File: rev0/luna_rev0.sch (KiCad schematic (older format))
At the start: 37 parts, among them J1 USB_B_Micro, J2 USB_B_Micro, J3 USB_A, J4 USB_B_Micro, J7 Conn_02x02_Counter_Clockwise, J8 Conn_Coaxial, J9 Conn_Coaxial, SW1 BTN_DFU, SW2 BTN_RESET, U1 AP22814-SOT, U12 AP22814-SOT, Y1 Osc60MHz

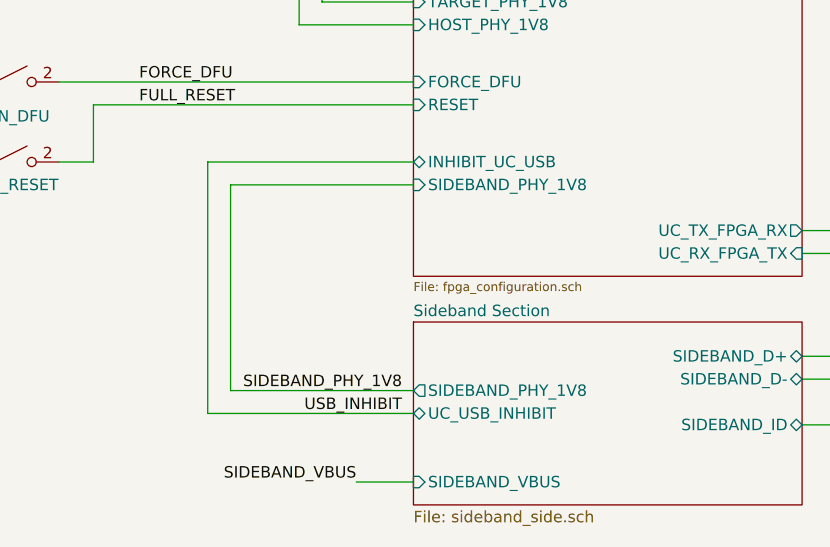
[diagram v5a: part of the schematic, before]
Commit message: hardware: add FPGA self-program option
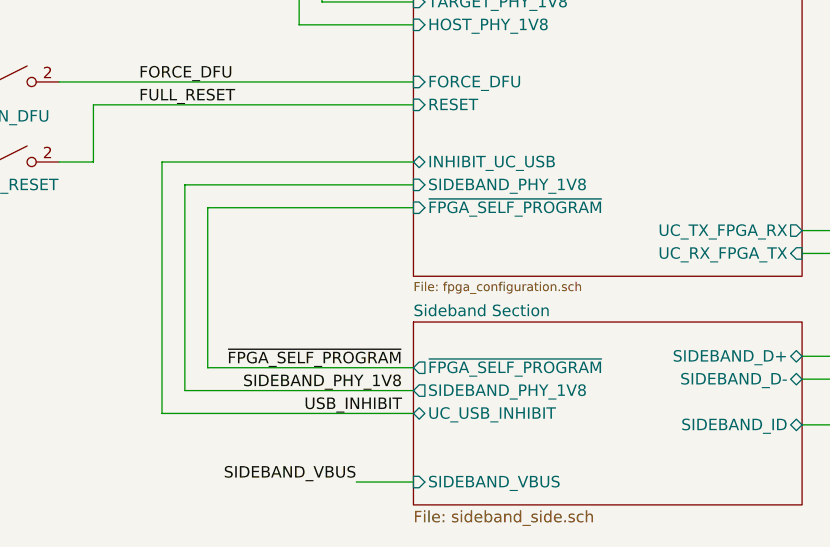
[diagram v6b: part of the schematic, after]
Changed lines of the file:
@@
 F1 "power_supplies.sch" 50
-$EndSheet
-$Sheet
-S 4000 4900 1700 1500
-U 5DCAA6D2
-F0 "FPGA Configuration and Dev Features" 39
-F1 "fpga_configuration.sch" 39
-F2 "SIDEBAND_D-" B R 5700 5150 50
-F3 "SIDEBAND_D+" B R 5700 5050 50
-F4 "SIDEBAND_PHY_1V8" I L 4000 6000 50
-F5 "HOST_PHY_1V8" I L 4000 5300 50
-F6 "TARGET_PHY_1V8" I L 4000 5200 50
-F7 "FORCE_DFU" I L 4000 5550 50
-F8 "INHIBIT_UC_USB" B L 4000 5900 50
-F9 "RESET" I L 4000 5650 50
-F10 "UC_TX_FPGA_RX" O R 5700 6200 50
-F11 "UC_RX_FPGA_TX" I R 5700 6300 50
 $EndSheet
 Text Label 5950 5050 0    50   ~ 0
@@
 F6 "SIDEBAND_ID" B R 5700 7050 50
 F7 "UC_USB_INHIBIT" B L 4000 7000 50
+F8 "~FPGA_SELF_PROGRAM" O L 4000 6800 50
 $EndSheet
 Wire Wire Line
-	4000 6900 3200 6900
+	4000 6900 3000 6900
 Wire Wire Line
 	6500 4850 6500 4600
@@
 $EndComp
 Wire Wire Line
-	3200 6900 3200 6000
+	3000 6900 3000 6000
 Wire Wire Line
 	3500 5300 4000 5300
@@
 HOST_ID
 Wire Wire Line
-	4000 6000 3200 6000
+	4000 6000 3000 6000
 $Comp
 L Switch:SW_SPST SW1
@@
 $EndSheet
 Wire Wire Line
-	4000 7000 3100 7000
-Wire Wire Line
-	3100 7000 3100 5900
-Wire Wire Line
-	3100 5900 4000 5900
+	4000 7000 2900 7000
+Wire Wire Line
+	2900 7000 2900 5900
+Wire Wire Line
+	2900 5900 4000 5900
 Text Label 3950 7000 2    50   ~ 0
 USB_INHIBIT
@@
 Wire Wire Line
 	9750 5750 9950 5750
+$Sheet
+S 4000 4900 1700 1500
+U 5DCAA6D2
+F0 "FPGA Configuration and Dev Features" 39
+F1 "fpga_configuration.sch" 39
+F2 "SIDEBAND_D-" B R 5700 5150 50
+F3 "SIDEBAND_D+" B R 5700 5050 50
+F4 "SIDEBAND_PHY_1V8" I L 4000 6000 50
+F5 "HOST_PHY_1V8" I L 4000 5300 50
+F6 "TARGET_PHY_1V8" I L 4000 5200 50
+F7 "FORCE_DFU" I L 4000 5550 50
+F8 "INHIBIT_UC_USB" B L 4000 5900 50
+F9 "RESET" I L 4000 5650 50
+F10 "UC_TX_FPGA_RX" O R 5700 6200 50
+F11 "UC_RX_FPGA_TX" I R 5700 6300 50
+F12 "~FPGA_SELF_PROGRAM" I L 4000 6100 50
+$EndSheet
+Wire Wire Line
+	4000 6800 3100 6800
+Wire Wire Line
+	3100 6800 3100 6100
+Wire Wire Line
+	3100 6100 4000 6100
+Text Label 3950 6800 2    50   ~ 0
+~FPGA_SELF_PROGRAM
 $EndSCHEMATC

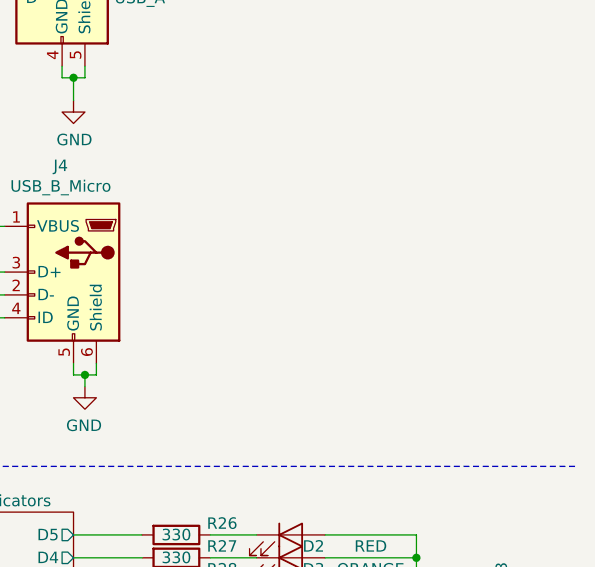
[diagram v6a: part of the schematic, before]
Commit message: hardware: change J3 part selection to Jing C42504
Footprint is designed for Kycon KUSBXHT-SB-AS1N-B30-NF in order to fit a
wide variety of compatible parts.
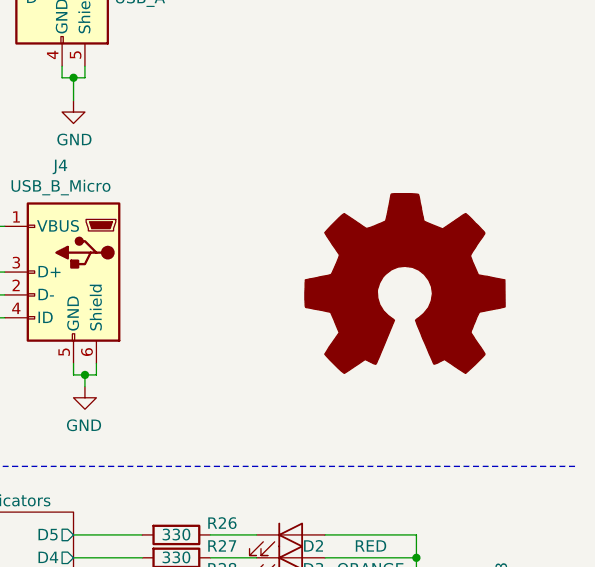
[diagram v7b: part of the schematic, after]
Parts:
- J3: footprint luna:CONN-Amphenol-UE27AC54100 -> luna:USB_A_Kycon_KUSBXHT-SB-AS1N-B30-NF_Horizontal; Description CONN RCPT USB2.0 TYPEA 4POS R/A -> USB A TYPE RECEPTACLE, SHORT BODY; Manufacturer Amphenol ICC -> Jing Extension of the Electronic Co.; Part Number UE27AC54100 -> C42504
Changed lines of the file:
@@
 Sheet 1 9
 Title "LUNA USB Multitool"
-Date "2020-05-21"
+Date "2020-12-07"
 Rev "r0"
 Comp "Copyright 2019-2020 Great Scott Gadgets"
@@
 Wire Wire Line
 	8950 2850 8950 2900
-$Comp
-L Connector:USB_A J3
-U 1 1 5DD6DEF2
-P 8950 2450
-F 0 "J3" H 8721 2439 50  0000 R CNN
-F 1 "USB_A" H 8721 2349 50  0000 R CNN
-F 2 "luna:CONN-Amphenol-UE27AC54100" H 9100 2400 50  0001 C CNN
-F 3 " ~" H 9100 2400 50  0001 C CNN
-F 4 "CONN RCPT USB2.0 TYPEA 4POS R/A" H 8950 2450 50  0001 C CNN "Description"
-F 5 "Amphenol ICC" H 8950 2450 50  0001 C CNN "Manufacturer"
-F 6 "UE27AC54100" H 8950 2450 50  0001 C CNN "Part Number"
-	1    8950 2450
-	-1   0    0    -1
-$EndComp
 Wire Wire Line
 	4000 3500 3600 3500
@@
 Text Label 3950 6800 2    50   ~ 0
 ~FPGA_SELF_PROGRAM
+$Comp
+L Graphic:Logo_Open_Hardware_Large #LOGO1
+U 1 1 5FCC45F6
+P 10450 3850
+F 0 "#LOGO1" H 10450 4350 50  0001 C CNN
+F 1 "Logo_Open_Hardware_Large" H 10450 3450 50  0001 C CNN
+F 2 "" H 10450 3850 50  0001 C CNN
+F 3 "~" H 10450 3850 50  0001 C CNN
+	1    10450 3850
+	1    0    0    -1
+$EndComp
+$Comp
+L Connector:USB_A J3
+U 1 1 5DD6DEF2
+P 8950 2450
+F 0 "J3" H 8721 2439 50  0000 R CNN
+F 1 "USB_A" H 8721 2349 50  0000 R CNN
+F 2 "luna:USB_A_Kycon_KUSBXHT-SB-AS1N-B30-NF_Horizontal" H 9100 2400 50  0001 C CNN
+F 3 " ~" H 9100 2400 50  0001 C CNN
+F 4 "USB A TYPE RECEPTACLE, SHORT BODY" H 8950 2450 50  0001 C CNN "Description"
+F 5 "Jing Extension of the Electronic Co." H 8950 2450 50  0001 C CNN "Manufacturer"
+F 6 "C42504" H 8950 2450 50  0001 C CNN "Part Number"
+	1    8950 2450
+	-1   0    0    -1
+$EndComp
 $EndSCHEMATC

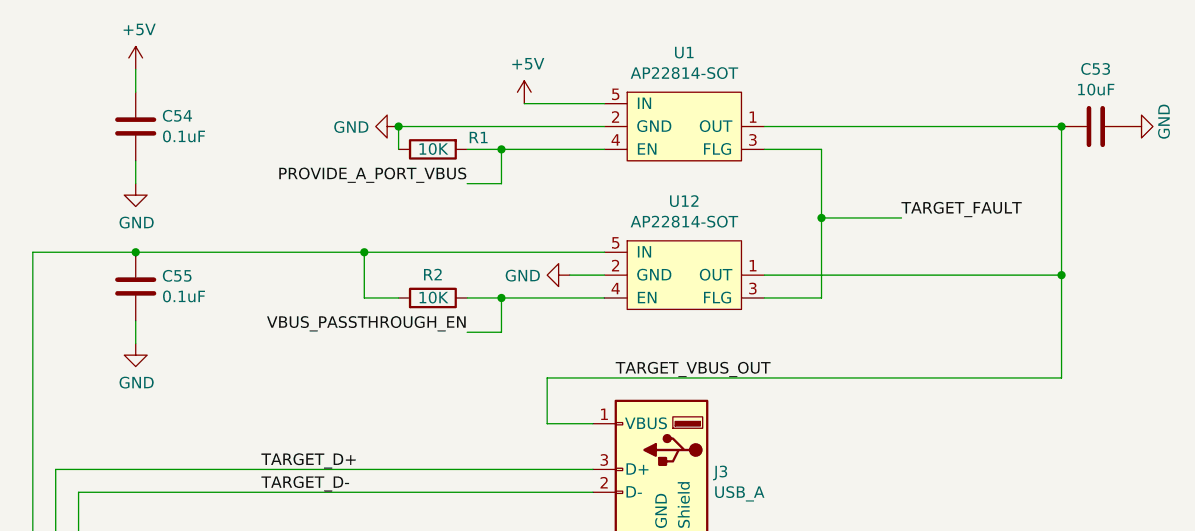
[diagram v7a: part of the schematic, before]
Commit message: hardware: fix load switch oscillation by decreasing R1 and R2 values
update load switch input and output capacitors
add GND zone on In2.Cu under J3 data signals
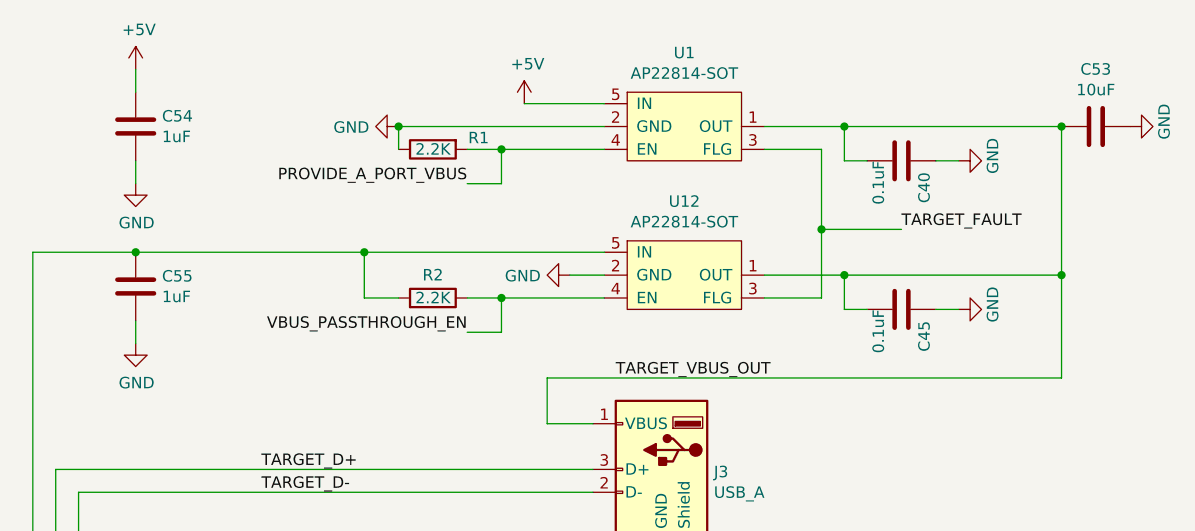
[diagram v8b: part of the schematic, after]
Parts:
- added C40, C45: 0.1uF, Capacitor_SMD:C_0402_1005Metric, symbol Device:C
- C54, C55: value 0.1uF -> 1uF; footprint Capacitor_SMD:C_0402_1005Metric -> Capacitor_SMD:C_0603_1608Metric; Part Number GENERIC-CAP-0402-0.1uF -> GENERIC-CAP-0603-1uF
- R1, R2: value 10K -> 2.2K; Part Number GENERIC-RES-0402-10K -> GENERIC-RES-0402-2.2K
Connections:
- net GND: now also C40.1, C45.1
- net TARGET_VBUS_OUT: now also C40.2, C45.2
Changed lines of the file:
@@
 Wire Wire Line
 	8550 1600 8700 1600
-Text Label 10000 1350 0    50   ~ 0
+Text Label 10000 1400 0    50   ~ 0
 TARGET_FAULT
 Text Label 8100 1200 2    50   ~ 0
@@
 P 7950 1700
 F 0 "R2" V 8050 1700 50  0000 C CNN
-F 1 "10K" V 7950 1700 50  0000 C CNN
+F 1 "2.2K" V 7950 1700 50  0000 C CNN
 F 2 "Resistor_SMD:R_0402_1005Metric" V 7880 1700 50  0001 C CNN
 F 3 "~" H 7950 1700 50  0001 C CNN
-F 4 "GENERIC-RES-0402-10K" H 7950 1700 50  0001 C CNN "Part Number"
+F 4 "GENERIC-RES-0402-2.2K" H 7950 1700 50  0001 C CNN "Part Number"
 	1    7950 1700
 	0    1    -1   0
@@
 $EndComp
 Wire Wire Line
-	9400 1600 10700 1600
+	9400 1600 9750 1600
 Wire Wire Line
 	10700 1600 10700 2050
@@
 P 7950 1050
 F 0 "R1" V 7900 850 50  0000 C CNN
-F 1 "10K" V 7950 1050 50  0000 C CNN
+F 1 "2.2K" V 7950 1050 50  0000 C CNN
 F 2 "Resistor_SMD:R_0402_1005Metric" V 7880 1050 50  0001 C CNN
 F 3 "~" H 7950 1050 50  0001 C CNN
-F 4 "GENERIC-RES-0402-10K" H 7950 1050 50  0001 C CNN "Part Number"
+F 4 "GENERIC-RES-0402-2.2K" H 7950 1050 50  0001 C CNN "Part Number"
 	1    7950 1050
 	0    -1   1    0
@@
 	8100 1050 8250 1050
 Wire Wire Line
-	9400 950  10700 950
+	9400 950  9750 950
 Wire Wire Line
 	10700 950  10700 1600
@@
 Connection ~ 7800 950
 Wire Wire Line
-	9650 1050 9650 1350
+	9650 1050 9650 1400
 Wire Wire Line
 	9400 1050 9650 1050
@@
 	9400 1700 9650 1700
 Wire Wire Line
-	9650 1700 9650 1350
-Connection ~ 9650 1350
-Wire Wire Line
-	9650 1350 10000 1350
+	9650 1700 9650 1400
+Connection ~ 9650 1400
+Wire Wire Line
+	9650 1400 10000 1400
 $Comp
 L Device:R R3
@@
 P 6650 950
 F 0 "C54" H 6765 995 50  0000 L CNN
-F 1 "0.1uF" H 6765 905 50  0000 L CNN
-F 2 "Capacitor_SMD:C_0402_1005Metric" H 6688 800 50  0001 C CNN
+F 1 "1uF" H 6765 905 50  0000 L CNN
+F 2 "Capacitor_SMD:C_0603_1608Metric" H 6688 800 50  0001 C CNN
 F 3 "~" H 6650 950 50  0001 C CNN
-F 4 "GENERIC-CAP-0402-0.1uF" H 6650 950 50  0001 C CNN "Part Number"
+F 4 "GENERIC-CAP-0603-1uF" H 6650 950 50  0001 C CNN "Part Number"
 	1    6650 950
 	1    0    0    -1
@@
 P 6650 1650
 F 0 "C55" H 6765 1695 50  0000 L CNN
-F 1 "0.1uF" H 6765 1605 50  0000 L CNN
-F 2 "Capacitor_SMD:C_0402_1005Metric" H 6688 1500 50  0001 C CNN
+F 1 "1uF" H 6765 1605 50  0000 L CNN
+F 2 "Capacitor_SMD:C_0603_1608Metric" H 6688 1500 50  0001 C CNN
 F 3 "~" H 6650 1650 50  0001 C CNN
-F 4 "GENERIC-CAP-0402-0.1uF" H 6650 1650 50  0001 C CNN "Part Number"
+F 4 "GENERIC-CAP-0603-1uF" H 6650 1650 50  0001 C CNN "Part Number"
 	1    6650 1650
 	1    0    0    -1
@@
 	-1   0    0    -1
 $EndComp
+$Comp
+L Device:C C?
+U 1 1 5FD2DC1A
+P 10000 1750
+AR Path="/5DA7BAF4/5FD2DC1A" Ref="C?"  Part="1"
+AR Path="/5FD2DC1A" Ref="C45"  Part="1"
+F 0 "C45" H 10050 1850 50  0000 L CNN
+F 1 "0.1uF" H 10000 1650 50  0000 L CNN
+F 2 "Capacitor_SMD:C_0402_1005Metric" H 10038 1600 50  0001 C CNN
+F 3 "~" H 10000 1750 50  0001 C CNN
+F 4 "GENERIC-CAP-0402-0.1uF" H 10000 1750 50  0001 C CNN "Part Number"
+	1    10000 1750
+	0    1    1    0
+$EndComp
+$Comp
+L Device:C C?
+U 1 1 5FD45580
+P 10000 1100
+AR Path="/5DA7BAF4/5FD45580" Ref="C?"  Part="1"
+AR Path="/5FD45580" Ref="C40"  Part="1"
+F 0 "C40" H 10050 1200 50  0000 L CNN
+F 1 "0.1uF" H 10000 1000 50  0000 L CNN
+F 2 "Capacitor_SMD:C_0402_1005Metric" H 10038 950 50  0001 C CNN
+F 3 "~" H 10000 1100 50  0001 C CNN
+F 4 "GENERIC-CAP-0402-0.1uF" H 10000 1100 50  0001 C CNN "Part Number"
+	1    10000 1100
+	0    1    1    0
+$EndComp
+Wire Wire Line
+	9750 950  9750 1100
+Wire Wire Line
+	9750 1100 9850 1100
+Connection ~ 9750 950
+Wire Wire Line
+	9750 950  10700 950
+Wire Wire Line
+	9750 1600 9750 1750
+Wire Wire Line
+	9750 1750 9850 1750
+Connection ~ 9750 1600
+Wire Wire Line
+	9750 1600 10700 1600
+$Comp
+L power:GND #PWR03
+U 1 1 5FD5A029
+P 10250 1100
+F 0 "#PWR03" H 10250 850 50  0001 C CNN
+F 1 "GND" H 10350 950 50  0000 R CNN
+F 2 "" H 10250 1100 50  0001 C CNN
+F 3 "" H 10250 1100 50  0001 C CNN
+	1    10250 1100
+	0    -1   -1   0
+$EndComp
+$Comp
+L power:GND #PWR07
+U 1 1 5FD5A3AD
+P 10250 1750
+F 0 "#PWR07" H 10250 1500 50  0001 C CNN
+F 1 "GND" H 10350 1600 50  0000 R CNN
+F 2 "" H 10250 1750 50  0001 C CNN
+F 3 "" H 10250 1750 50  0001 C CNN
+	1    10250 1750
+	0    -1   -1   0
+$EndComp
+Wire Wire Line
+	10250 1750 10150 1750
+Wire Wire Line
+	10150 1100 10250 1100
 $EndSCHEMATC
